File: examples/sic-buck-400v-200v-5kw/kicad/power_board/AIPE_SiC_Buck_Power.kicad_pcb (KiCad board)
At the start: 4 copper layers, 240 x 180 mm, 237 parts, among them J1 VIN_RAW (+IN), J2 PGND (-IN), J3 VOUT (+OUT), J4 PGND (-OUT), J5 RLY_A (VIN_RAW), J6 RLY_B (VIN), J7 Mezzanine 2x25 socket, J8 FAN 12V/GND/TACH, J9 Relay coil K1, Q1 C4MS025120K, Q2 C4MS025120K, Q3 AO3400A, U1 UCC21710QDWRQ1, U10 TMCS1133C2AQDVGR, U2 UCC14141QDWNRQ1, U3 UCC21710QDWRQ1, U4 UCC14141QDWNRQ1, U5 UCC14141QDWNRQ1, U6 AMC1311BDWVR, U7 AMC1311BDWVR, U8 OPA2320AIDGKR, U9 REF3125AIDBZR

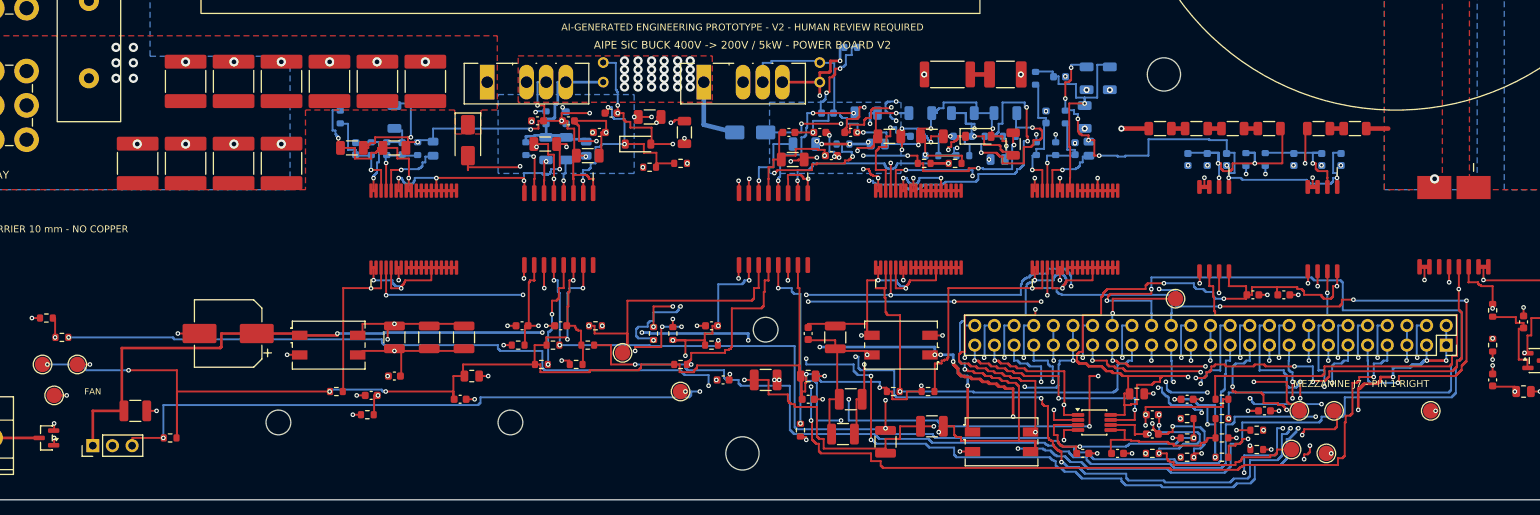
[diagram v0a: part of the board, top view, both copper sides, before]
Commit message: feat(v2.1): example regenerated - wired schematics, both boards routed with the upgraded router, exports, crops, validation
Schematics (wired style, gates passed): ERC 0 on both projects (power 20261012T075113Z-erc-df18ce6e,
control 20261012T075120Z-erc-7a14cacb); netlist (ref,pad)->net exact vs the model and vs the frozen V2
netlists with equal net names; .kicad_dru / net_settings identical to the legacy generation; stub
global labels 648 -> 7 (power) and 667 -> 7 (control), wired pin share 0 -> 0.90 / 0.76, junctions,
hierarchical labels and power symbols introduced, continuation sheets removed; readability metrics
V2 vs V2.1 in engineering_checks/schematic_readability_*.

Power board (octilinear simplification + tangent arcs on the V2 search; 8-direction search kept
opt-in after attempt A left 2 connections open): 0 unresolved, DRC 0/0/0 (20261012T090308Z-drc-8fd50803),
segments 4755 -> 2991 + 145 arcs, 90-degree bends 3609 -> 1121, stair runs 382 -> 124, length
5744.6 -> 5545.6 mm, vias 606 = V2, no net longer / more vias / narrower. Control board: 0 unresolved,
DRC 0/0/0 (20261012T084327Z-drc-7f07f983), segments 5995 -> 4262 + 261 arcs, 90-degree bends
4069 -> 1233, stair runs 435 -> 144, length 7055.2 -> 6700.7 mm, vias 798 = V2, 96 nets shorter,
0 longer. FOOTPRINT.SetDNP for DNP parts (schematic parity), beautify anchors bound to off-grid vias
by copper overlap (path_geometry.connected_by_overlap), In2.Cu inner pass styled.

Exports 11/11 per board, renders and layer PDFs refreshed, high-resolution V2/V2.1 crops under
review/crops/, routing_quality_* and v21_validation.{json,md} (nine TASK 7 checks independently
re-derived). verify_sic_buck passed; 338 tests OK (2 skipped).

Co-Authored-By: Claude Fable 5.1 <noreply@anthropic.com>
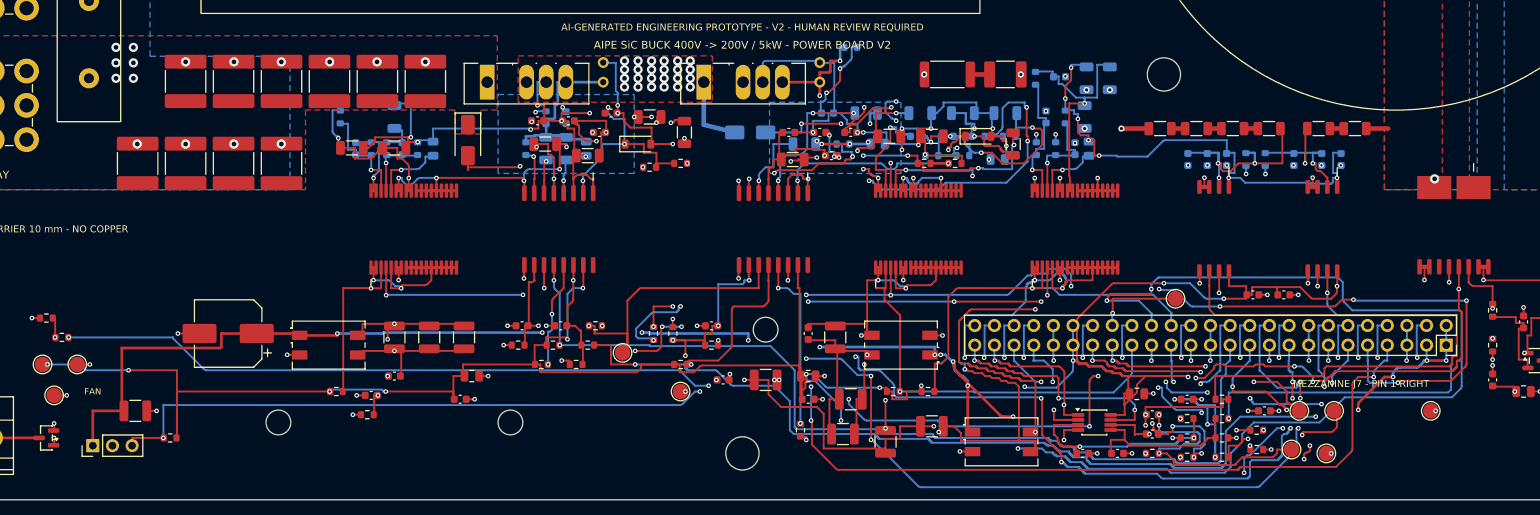
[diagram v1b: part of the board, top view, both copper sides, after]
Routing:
- net 3V3: track 433.9 -> 417.8 mm
- net 12V_PROT: track 276.6 -> 261.8 mm
- net FLT_H_N: track 166.3 -> 154.6 mm
- net PG_BIAS_H_N: track 268.5 -> 256.9 mm
- net FLT_L_N: track 120.0 -> 111.1 mm
- net RELAY_ON: track 203.9 -> 195.8 mm
- net PWM_H: track 132.3 -> 124.9 mm
- net LS_FB_VDD: track 72.8 -> 66.4 mm
- net RESET_N: track 129.2 -> 123.4 mm
- net BIAS_EN: track 147.9 -> 142.4 mm
- net VEE_L: track 100.1 -> 94.8 mm
- net PWM_L: track 111.6 -> 106.7 mm
- net RDY_L: track 112.3 -> 107.4 mm
- net GNDP_S: track 119.3 -> 114.9 mm
- net DESAT_L_OC: track 99.1 -> 94.8 mm
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
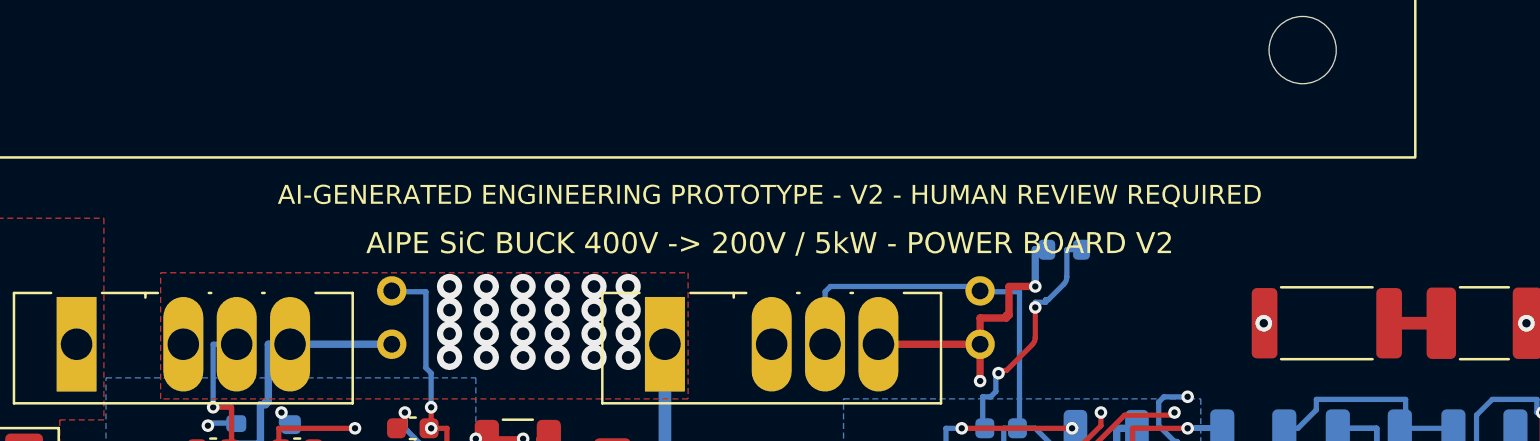
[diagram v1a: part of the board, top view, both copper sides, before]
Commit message: chore(v2.1): one generation label (sic_buck_common.GENERATION) and a reproducible full regeneration
GENERATION = "V2.1" derives BANNER, REVISION, title-block comments, .kicad_dru headers,
NOTICE.md, the power-board silkscreen and the control-board label (kept at the V2 label
length so the placer's text obstacle box, and therefore the placement, is unchanged).
Models, schematics (ERC 0: 20261012T094955Z-erc-c574a866 / 20261012T095007Z-erc-caa10a79,
all gates passed), both boards (DRC 0/0/0: power 20261012T100423Z-drc-8b9e64d1, control
20261012T103755Z-drc-0a4fa5cf), netlist checks, routing-quality records (totals, per-layer
and per-net tables identical to the previous commit), exports (11/11 each), renders, V2.1
crops (same framing; V2 crops untouched) and readability reports regenerated. Independent
re-validation in verification/v21_validation.{json,md} (12 rows). verify_sic_buck passed;
340 tests OK (2 skipped). Known residue: control-board corridor zone priorities depend on
reload order (same zones, DRC clean), manufacturing/README.md still describes the V2 bundle.

Co-Authored-By: Claude Fable 5.1 <noreply@anthropic.com>
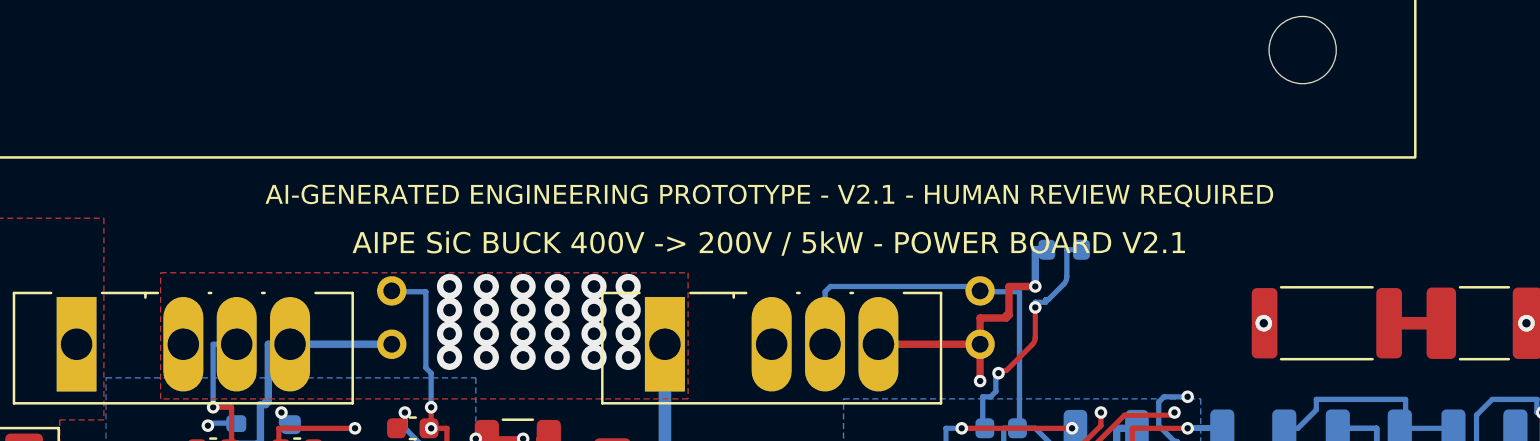
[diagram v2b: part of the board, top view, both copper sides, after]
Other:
- board text added: "AI-GENERATED ENGINEERING PROTOTYPE - V2.1 - HUMAN REVIEW REQUIRED"
- board text added: "AIPE SiC BUCK 400V -> 200V / 5kW - POWER BOARD V2.1"
- board text removed: "AI-GENERATED ENGINEERING PROTOTYPE - V2 - HUMAN REVIEW REQUIRED"
- board text removed: "AIPE SiC BUCK 400V -> 200V / 5kW - POWER BOARD V2"
